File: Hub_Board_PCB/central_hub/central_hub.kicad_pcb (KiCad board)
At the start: 2 copper layers, 92 parts, among them J1 CAN_OUT, J2 Barrel_Jack_MountingPin, J3 Screw_Terminal_01x08, J4 Screw_Terminal_01x08, J6 Screw_Terminal_01x06, J7 Screw_Terminal_01x04, J8 Conn_01x02, J9 Screw_Terminal_01x04, Q1 BSS138, Q2 BSS138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

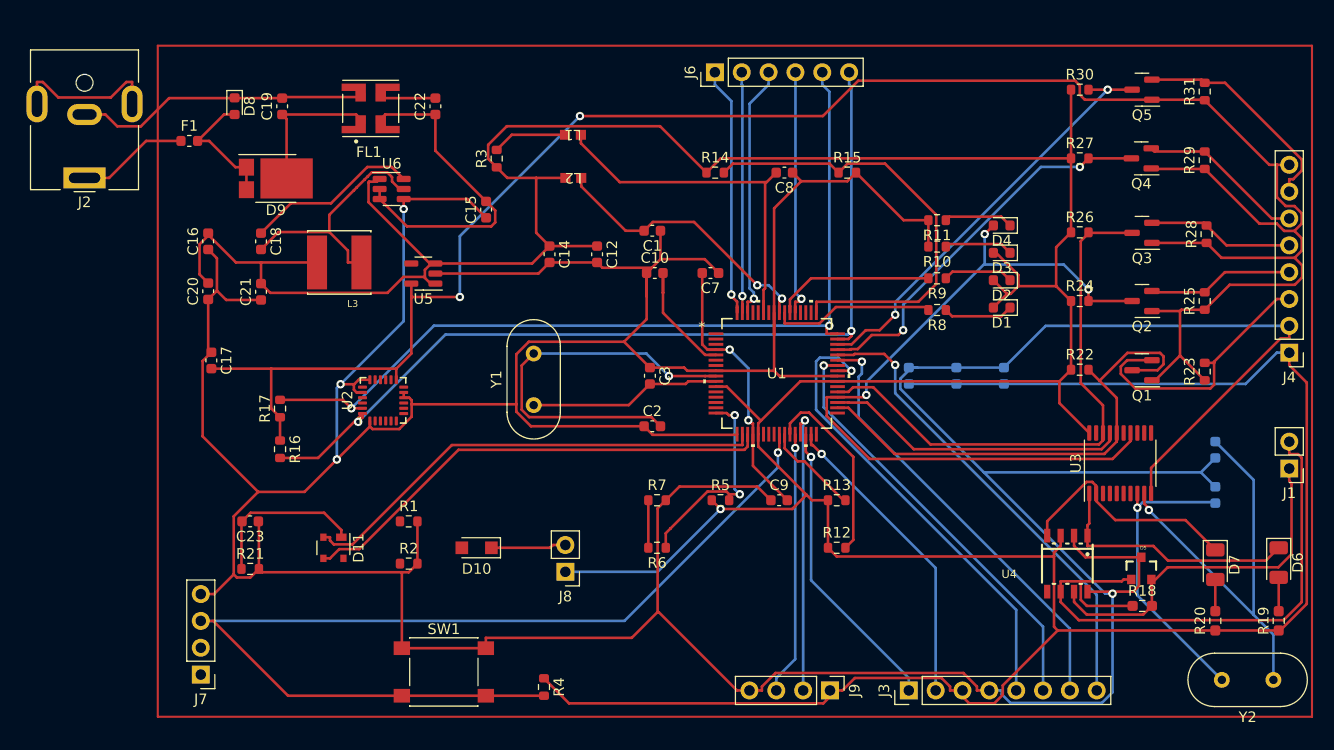
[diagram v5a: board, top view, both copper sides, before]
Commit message: Fixed PCB after last commit
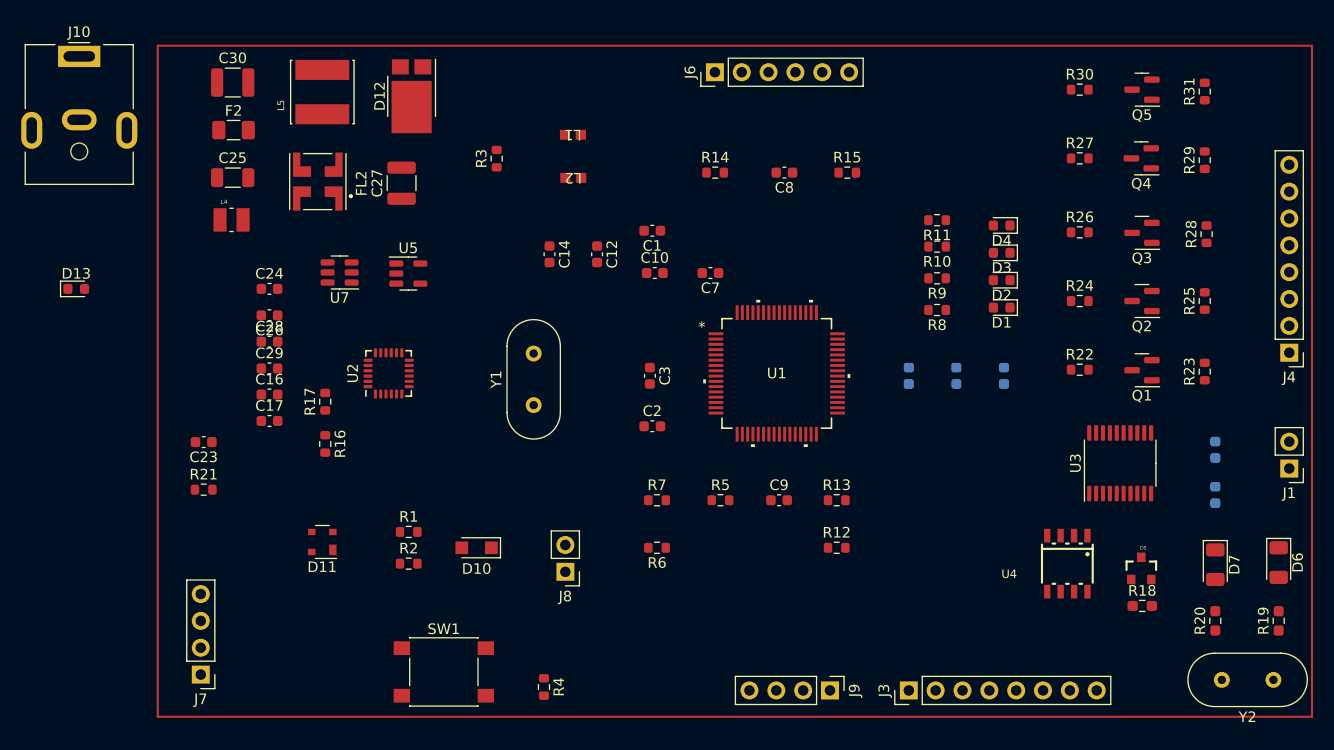
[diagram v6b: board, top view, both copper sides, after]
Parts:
- removed C15: 10u, Capacitor_SMD:C_0603_1608Metric
- removed C18: 100n, Capacitor_SMD:C_0603_1608Metric
- removed C19, C22: 100u, Capacitor_SMD:C_0603_1608Metric
- removed C20, C21: 22u, Capacitor_SMD:C_0603_1608Metric
- removed D8: 5.0SMDJ16CA, Diode_SMD:D_0603_1608Metric
- removed D9: PMEG030V050EPD, Package_TO_SOT_SMD:Nexperia_CFP15_SOT-1289
- removed F1: 0685T3000-01, Fuse:Fuse_0603_1608Metric
- removed FL1: DLW5BTM251TQ2L, ~ALL:FIL_DLW5BTZ251TQ2L
- removed J2: Barrel_Jack_MountingPin, Connector_BarrelJack:BarrelJack_CUI_PJ-063AH_Horizontal
- removed L3: 4.7u, ~ALL:IND_VLS6045EX-100M
- removed U6: AP63205WU-7, Package_TO_SOT_SMD:TSOT-23-6
- added C24: 10u, Capacitor_SMD:C_0603_1608Metric, F.Cu at (189.5, 22.5)
- added C25: 1u, Capacitor_SMD:C_1206_3216Metric, F.Cu at (186.0, 12.0)
- added C26: 100n, Capacitor_SMD:C_0603_1608Metric, F.Cu at (189.5, 25.0)
- added C27: 10u, Capacitor_SMD:C_1210_3225Metric, F.Cu at (202.0, 12.5)
- added C28: 22u, Capacitor_SMD:C_0603_1608Metric, F.Cu at (189.5, 27.5)
- added C29: 22u, Capacitor_SMD:C_0603_1608Metric, F.Cu at (189.5, 30.0)
- added C30: 10u, Capacitor_SMD:C_1210_3225Metric, F.Cu at (186.0, 2.98)
- added D12: PMEG030V050EPD, Package_TO_SOT_SMD:Nexperia_CFP15_SOT-1289, F.Cu at (202.9, 4.28)
- added D13: 5.0SMDJ16CA, Diode_SMD:D_0603_1608Metric, F.Cu at (171.2, 22.5)
- added F2: 0685T3000-01, Fuse:Fuse_1206_3216Metric, F.Cu at (186.1, 7.47)
- added FL2: DLW5BTM251TQ2L, ~ALL:FIL_DLW5BTZ251TQ2L, F.Cu at (194.1, 12.3)
- added J10: Barrel_Jack_MountingPin, Connector_BarrelJack:BarrelJack_CUI_PJ-063AH_Horizontal, F.Cu at (171.5, 0.50)
- added L4: DFE252012F-4R7M=P2, ~ALL:INDC2520X120N, F.Cu at (185.9, 16.0)
- added L5: VLS6045EX-100M, ~ALL:IND_VLS6045EX-100M, F.Cu at (194.5, 3.88)
- added U7: AP63205WU-7, Package_TO_SOT_SMD:TSOT-23-6, F.Cu at (196.1, 20.9)
- moved C16 15.6 mm to (189.5, 32.5), turned to 0 degrees
- moved C23 8.70 mm to (183.3, 37.0)
- moved R21 8.70 mm to (183.3, 41.5)
- moved C17 7.94 mm to (189.5, 35.0), turned to 0 degrees
- moved R17 4.32 mm to (194.8, 33.2)
- moved R16 4.30 mm to (194.8, 37.2)
- moved U2 2.60 mm to (200.8, 30.5)
- moved U5 1.43 mm to (202.6, 21.1), turned to 0 degrees
- moved D11 1.19 mm to (194.5, 46.5), turned to 180 degrees
- moved R1 1.00 mm to (202.7, 45.5)
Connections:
- C1 pad 1: GND -> +12V
- C10 pad 1: GND -> +12V
- C11 pad 1: GND -> +12V
- C12 pad 2: GND -> +12V
- C13 pad 1: GND -> +12V
- C14 pad 2: GND -> +12V
- C16 pad 1: GND -> +12V
- C17 pad 1: GND -> +12V
- C2 pad 1: GND -> +12V
- C23 pad 1: GND -> +12V
- C3 pad 1: GND -> +12V
- C4 pad 1: GND -> +12V
- C5 pad 1: GND -> +12V
- C6 pad 1: GND -> +12V
- C7 pad 1: GND -> +12V
- C8 pad 1: GND -> +12V
- C9 pad 1: GND -> +12V
- D5 pad 3: GND -> +12V
- J3 pad 4: GND -> +12V
- J4 pad 2: GND -> +12V
- J7 pad 4: GND -> +12V
- J9 pad 4: GND -> +12V
- R1 pad 2: GND -> +12V
- R10 pad 2: GND -> +12V
- R11 pad 2: GND -> +12V
- R15 pad 2: GND -> +12V
- R2 pad 2: GND -> +12V
- R21 pad 2: GND -> +12V
- R7 pad 2: GND -> +12V
- SW1 pad 1: GND -> +12V
- U1 pad 17: GND -> +12V
- U1 pad 40: GND -> +12V
- U1 pad 57: GND -> +12V
- U1 pad 8: GND -> +12V
- U2 pad 1: GND -> +12V
- U2 pad 10: GND -> +12V
- U2 pad 11: GND -> +12V
- U2 pad 18: GND -> +12V
- U2 pad 20: GND -> +12V
- U3 pad 10: GND -> +12V
- U4 pad 2: GND -> +12V
- U4 pad 8: GND -> +12V
- U5 pad 2: GND -> +12V
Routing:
- net GND: track 525.5 -> 0.00 mm, vias 4 -> 0
- net +5V: track 440.9 -> 0.00 mm, vias 1 -> 0
- net +3.3V: track 203.1 -> 0.00 mm, vias 2 -> 0
- net ~{RESET}: track 100.0 -> 0.00 mm, vias 1 -> 0
- net A4: track 87.2 -> 0.00 mm, vias 2 -> 0
- net A5: track 82.7 -> 0.00 mm, vias 2 -> 0
- net D13: track 74.6 -> 0.00 mm, vias 3 -> 0
- net /CAN/CAN_LOW: track 56.0 -> 0.00 mm
- net D10: track 52.7 -> 0.00 mm
- net D11: track 47.9 -> 0.00 mm
- net USB_D+: track 46.3 -> 0.00 mm
- net USB_D-: track 45.5 -> 0.00 mm
- net D3: track 44.6 -> 0.00 mm, vias 1 -> 0
- net D7: track 44.3 -> 0.00 mm, vias 1 -> 0
- net Net-(U1-GTIOC2A/AN016/P500): track 42.8 -> 0.00 mm
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
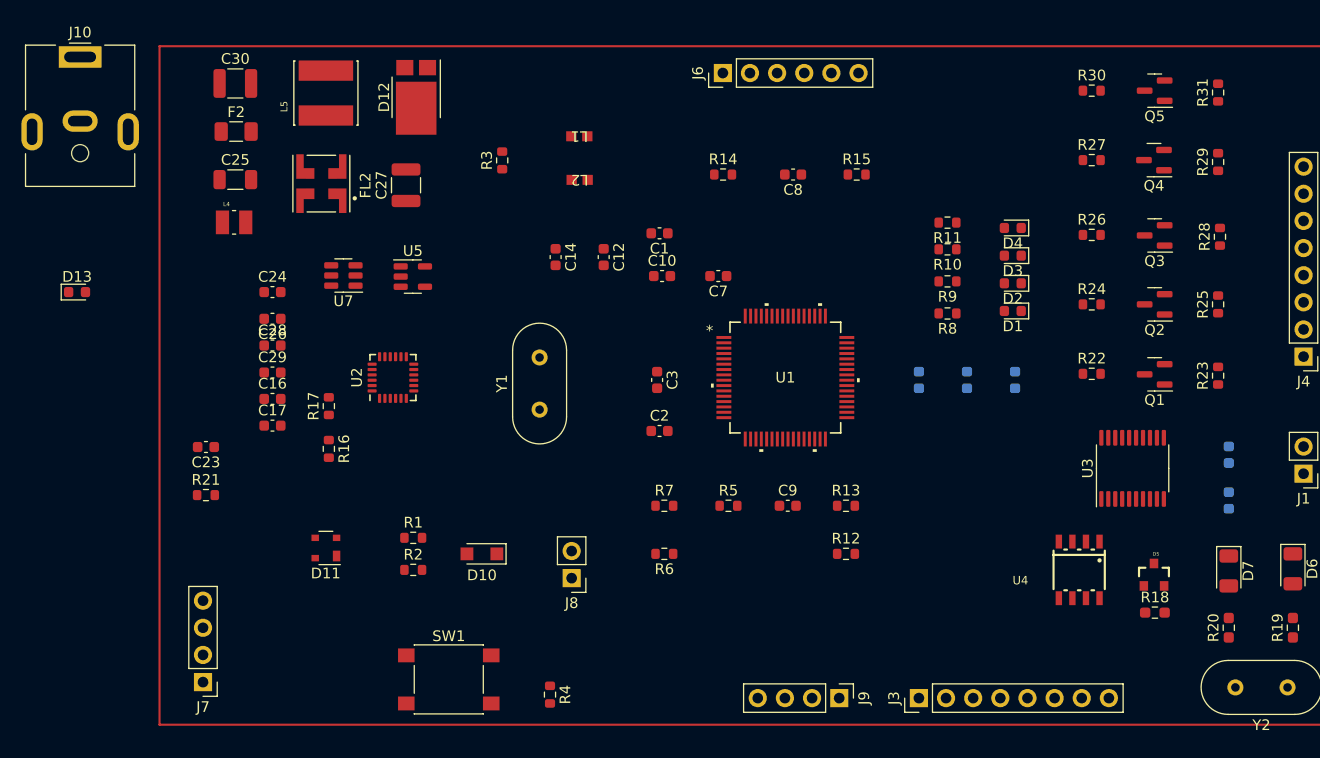
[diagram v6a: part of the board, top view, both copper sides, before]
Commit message: Added cap on accel chip and switched power connector
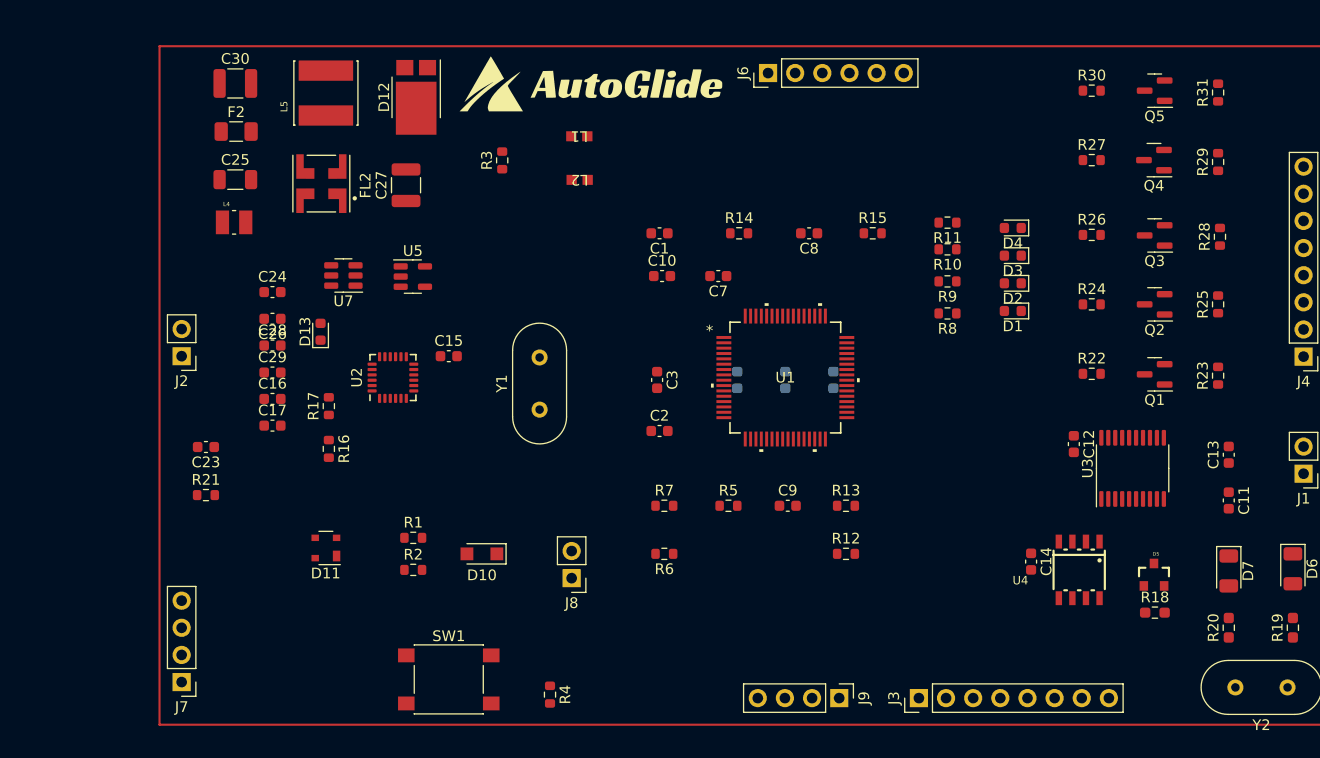
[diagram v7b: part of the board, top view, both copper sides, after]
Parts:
- removed J10: Barrel_Jack_MountingPin, Connector_BarrelJack:BarrelJack_CUI_PJ-063AH_Horizontal
- added C15: 0.1u, Capacitor_SMD:C_0603_1608Metric, F.Cu at (206.0, 28.5)
- added G***: LOGO, ~ALL:AutoGlideMedium, F.Cu at (219.5, 3.00)
- added J2: Conn_01x02, Connector_PinHeader_2.54mm:PinHeader_1x02_P2.54mm_Vertical, F.Cu at (181.0, 28.5)
- C11, C13: moved to F.Cu
- moved C14 52.8 mm to (260.5, 47.7)
- moved C12 47.4 mm to (264.5, 36.7)
- moved D13 23.1 mm to (194.0, 26.2), turned to 90 degrees
- moved C4 17.0 mm to (233.0, 30.7)
- moved C5 17.0 mm to (237.5, 30.7)
- moved C6 17.0 mm to (242.0, 30.7)
- moved C8 5.70 mm to (239.7, 17.0)
- moved R14 5.70 mm to (233.2, 17.0)
- moved R15 5.70 mm to (245.7, 17.0)
- moved J6 4.23 mm to (235.9, 2.00)
- moved J7 2.00 mm to (181.0, 59.0)
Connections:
- C1 pad 1: +12V -> GND
- C10 pad 1: +12V -> GND
- C11 pad 1: +12V -> GND
- C12 pad 2: +12V -> GND
- C13 pad 1: +12V -> GND
- C14 pad 2: +12V -> GND
- C16 pad 1: +12V -> GND
- C17 pad 1: +12V -> GND
- C2 pad 1: +12V -> GND
- C23 pad 1: +12V -> GND
- C24 pad 1: +12V -> GND
- C27 pad 1: +12V -> GND
- C28 pad 1: +12V -> GND
- C29 pad 1: +12V -> GND
- C3 pad 1: +12V -> GND
- C30 pad 1: +12V -> GND
- C4 pad 1: +12V -> GND
- C5 pad 1: +12V -> GND
- C6 pad 1: +12V -> GND
- C7 pad 1: +12V -> GND
- C8 pad 1: +12V -> GND
- C9 pad 1: +12V -> GND
- D13 pad 1: +12V -> GND
- D5 pad 3: +12V -> GND
- FL2 pad 3: +12V -> GND
- J3 pad 4: +12V -> GND
- J4 pad 2: +12V -> GND
- J7 pad 4: +12V -> GND
- J9 pad 4: +12V -> GND
- R1 pad 2: +12V -> GND
- R10 pad 2: +12V -> GND
- R11 pad 2: +12V -> GND
- R15 pad 2: +12V -> GND
- R2 pad 2: +12V -> GND
- R21 pad 2: +12V -> GND
- R7 pad 2: +12V -> GND
- SW1 pad 1: +12V -> GND
- U1 pad 17: +12V -> GND
- U1 pad 40: +12V -> GND
- U1 pad 57: +12V -> GND
- U1 pad 8: +12V -> GND
- U2 pad 1: +12V -> GND
- U2 pad 10: +12V -> GND
- U2 pad 11: +12V -> GND
- U2 pad 18: +12V -> GND
- U2 pad 20: +12V -> GND
- U3 pad 10: +12V -> GND
- U4 pad 2: +12V -> GND
- U4 pad 8: +12V -> GND
- U5 pad 2: +12V -> GND
- U7 pad 4: +12V -> GND

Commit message: Schematic changes before sending to kim
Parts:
- removed R7: 5.1k, Resistor_SMD:R_0603_1608Metric
- added C18: 0.1uF, Capacitor_SMD:C_0603_1608Metric, F.Cu at (228.3, -27.7)
- added C19: 2.2n, Capacitor_SMD:C_0603_1608Metric, F.Cu at (228.3, -25.1)
- added C31: 10n, Capacitor_SMD:C_0603_1608Metric, F.Cu at (228.3, -22.6)
- added J5: CSP-USC16-TR, ~ALL:VALCON_CSP-USC16-TR, F.Cu at (238.6, -27.6)
- added R32: 4.7k, Resistor_SMD:R_0603_1608Metric, F.Cu at (228.3, -20.1)
- added R33: 4.7k, Resistor_SMD:R_0603_1608Metric, F.Cu at (228.3, -17.6)
- added R34: 4.7k, Resistor_SMD:R_0603_1608Metric, F.Cu at (228.3, -15.1)
- added TP1: TestPoint, TestPoint:TestPoint_Pad_D1.0mm, F.Cu at (233.9, -15.9)
- added TP2: TestPoint, TestPoint:TestPoint_Pad_D1.0mm, F.Cu at (233.9, -12.9)
- added TP3: TestPoint, TestPoint:TestPoint_Pad_D1.0mm, F.Cu at (236.9, -15.9)
- added TP4: TestPoint, TestPoint:TestPoint_Pad_D1.0mm, F.Cu at (236.9, -12.9)
- added TP5: TestPoint, TestPoint:TestPoint_Pad_D1.0mm, F.Cu at (240.0, -15.9)
- added TP6: TestPoint, TestPoint:TestPoint_Pad_D1.0mm, F.Cu at (240.0, -12.9)
- added TP7: TestPoint, TestPoint:TestPoint_Pad_D1.0mm, F.Cu at (246.2, -27.4)
- added TP8: TestPoint, TestPoint:TestPoint_Pad_D1.0mm, F.Cu at (246.2, -24.3)
- added TP9: TestPoint, TestPoint:TestPoint_Pad_D1.0mm, F.Cu at (245.0, -15.9)
- C1, C5, C6, C9: value 15pF -> 100nF
- C10, C4: value 15pF -> 4.7uF
- C8: value 15pF -> 1uF
- J6: value Screw_Terminal_01x06 -> Screw_Terminal_01x04; footprint Connector_PinHeader_2.54mm:PinHeader_1x06_P2.54mm_Vertical -> Connector_PinHeader_2.54mm:PinHeader_1x04_P2.54mm_Vertical
- J7: value Screw_Terminal_01x04 -> Conn_01x03; footprint Connector_PinHeader_2.54mm:PinHeader_1x04_P2.54mm_Vertical -> Connector_PinHeader_2.54mm:PinHeader_1x03_P2.54mm_Vertical
- R6: value 5.1k -> 10k
- Y1: value 16MHz? -> 16MHz
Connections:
- J2 pad 1: -BATT -> +BATT
- J2 pad 2: +BATT -> -BATT
- J7 pad 1: IOREF -> BOOT
- J7 pad 2: BOOT -> ~{RESET}
- J7 pad 3: ~{RESET} -> GND
- R13 pad 2: /MCU/MD -> BOOT
- R16 pad 2: A4 -> SDA_Accel
- R17 pad 2: A5 -> SCL_Accel
- R6 pad 2: Net-(R6-Pad2) -> GND
- U1 pad 24: /MCU/P204 -> unconnected-(U1-GTIOC4B/P204-Pad24)
- U1 pad 26: /MCU/MD -> BOOT
- U1 pad 32: P300 -> unconnected-(U1-P300/GTIOC0A/TCK/SWCLK-Pad32)
- U1 pad 33: P108 -> unconnected-(U1-P108/GTIOC0B/TMS/SWDIO-Pad33)
- U1 pad 47: A4 -> SDA_Accel
- U1 pad 48: A5 -> SCL_Accel
- U1 pad 50: P501 -> unconnected-(U1-GTIOC2B/AN017/P501-Pad50)
- U1 pad 51: P502 -> unconnected-(U1-GTIOC3B/AN018/P502-Pad51)
- U2 pad 1: GND -> Net-(U2-CLKIN)
- U2 pad 10: GND -> Net-(U2-REGOUT)
- U2 pad 11: GND -> Net-(U2-FSYNC)
- U2 pad 20: GND -> Net-(U2-CPOUT)
- U2 pad 23: A5 -> SCL_Accel
- U2 pad 24: A4 -> SDA_Accel
- U2 pad 8: unconnected-(U2-VLOGIC-Pad8) -> +3.3V
- U2 pad 9: unconnected-(U2-AD0-Pad9) -> Net-(U2-AD0)
- U3 pad 19: unconnected-(U3-~{RESET}-Pad19) -> Net-(U3-~{RESET})
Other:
- board outline added: 0.6 x 1.7 mm
